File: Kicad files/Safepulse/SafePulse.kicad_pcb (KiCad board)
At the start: 4 copper layers, 40.6 x 20.8 mm, 90 parts, among them J1 Conn_01x03_Male, Q1 FQT7N10L, Q2 BC846A, Q3 MMBT3906, Q4 MMBT3906, U1 TS4061AILT-1.25, U2 74HC14, U3 TLV27L1DBVT, U33 MAX9910EXK+T, U4 CD14538BM

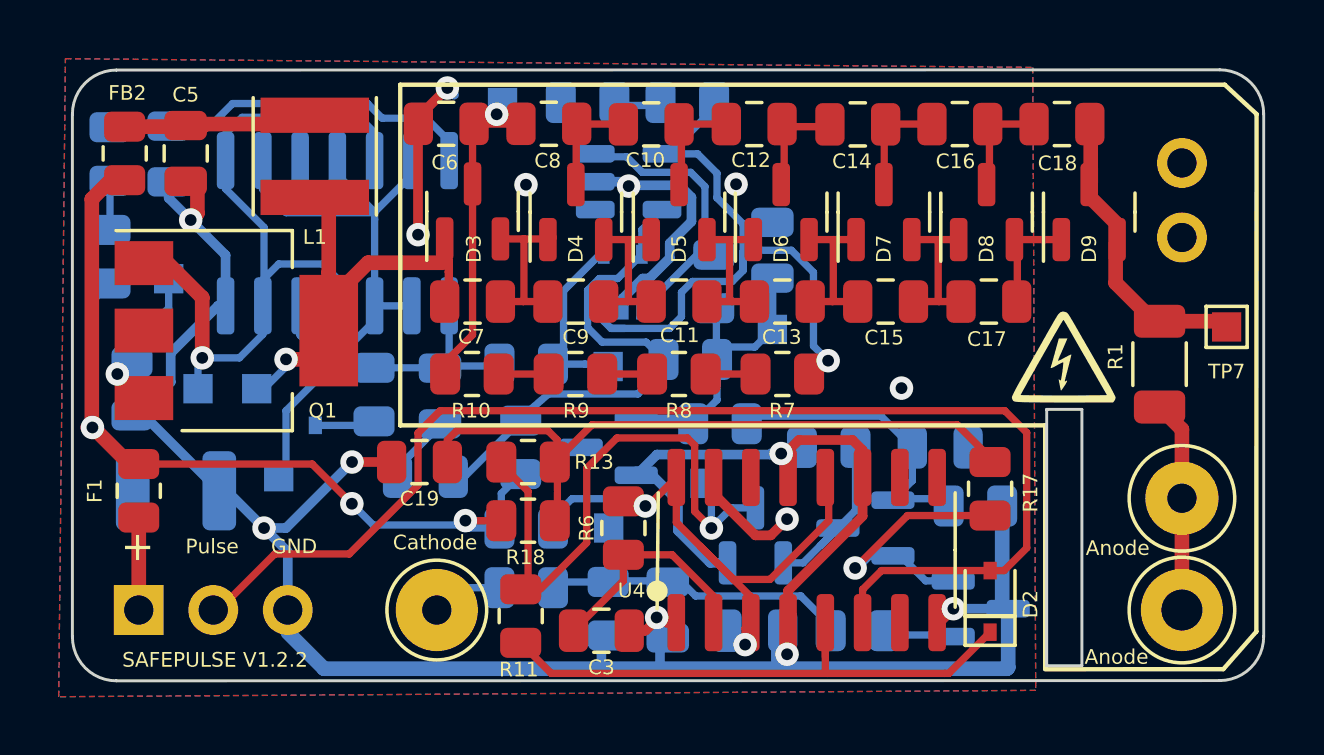
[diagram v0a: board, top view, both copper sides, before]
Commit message: Add initial production files for Safepulse project
- Created BOM file with components and specifications.
- Added designators for all components in designators.csv.
- Generated netlist in IPC format for circuit connections.
- Included positions of components in positions.csv for layout reference.
- Created lock file for PCB design session.
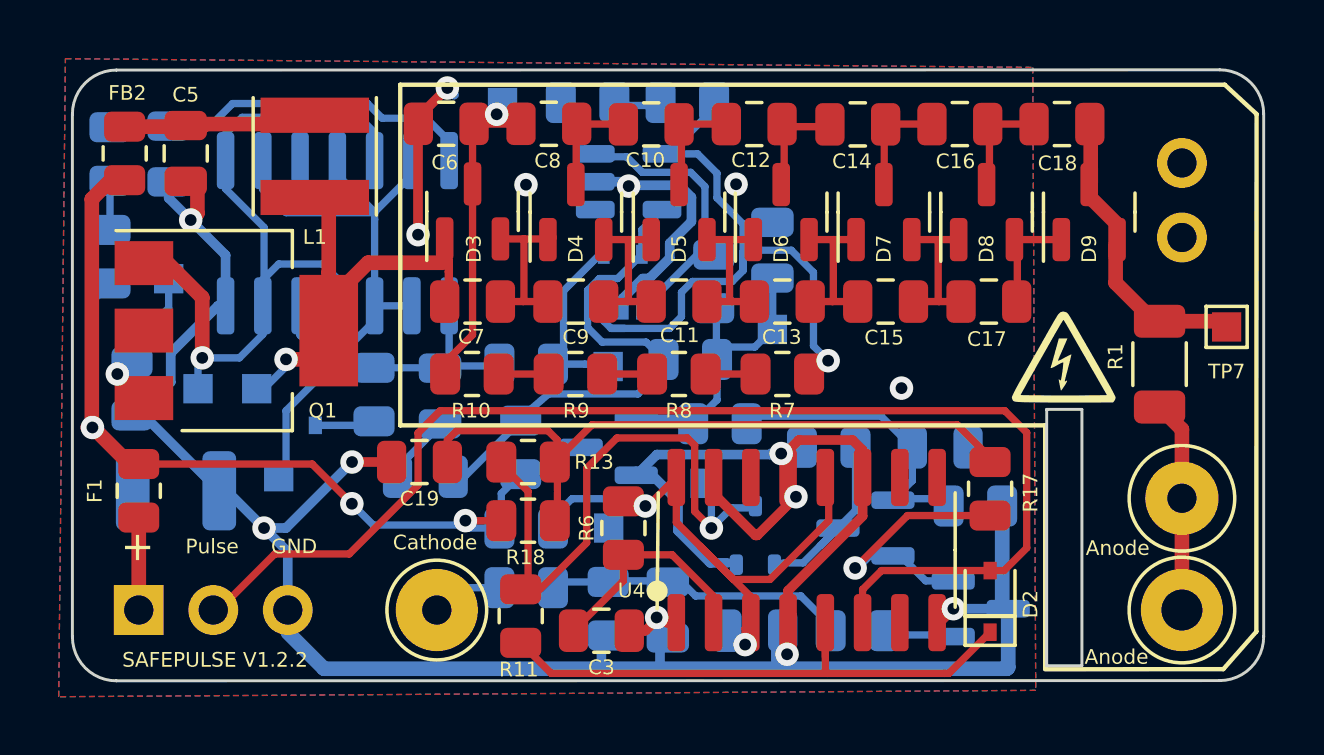
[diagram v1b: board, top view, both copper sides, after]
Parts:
- Q2: footprint Package_TO_SOT_SMD:SOT-23 -> Package_TO_SOT_SMD:SOT-323_SC-70

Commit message: Update V1.2.2
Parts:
- Q2: footprint Package_TO_SOT_SMD:SOT-323_SC-70 -> Package_TO_SOT_SMD:SOT-23
